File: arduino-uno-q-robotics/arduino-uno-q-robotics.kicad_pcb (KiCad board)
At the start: 4 copper layers, 68.6 x 53.3 mm, 15 parts, among them J1 Conn_02x30_Odd_Even, J2 Conn_02x30_Odd_Even, J3 Connector_FFC-FPC, J5 Conn_02x13_Odd_Even, J6 Conn_02x04_Odd_Even, U1 LSM6DSO32, U2 TCA9803

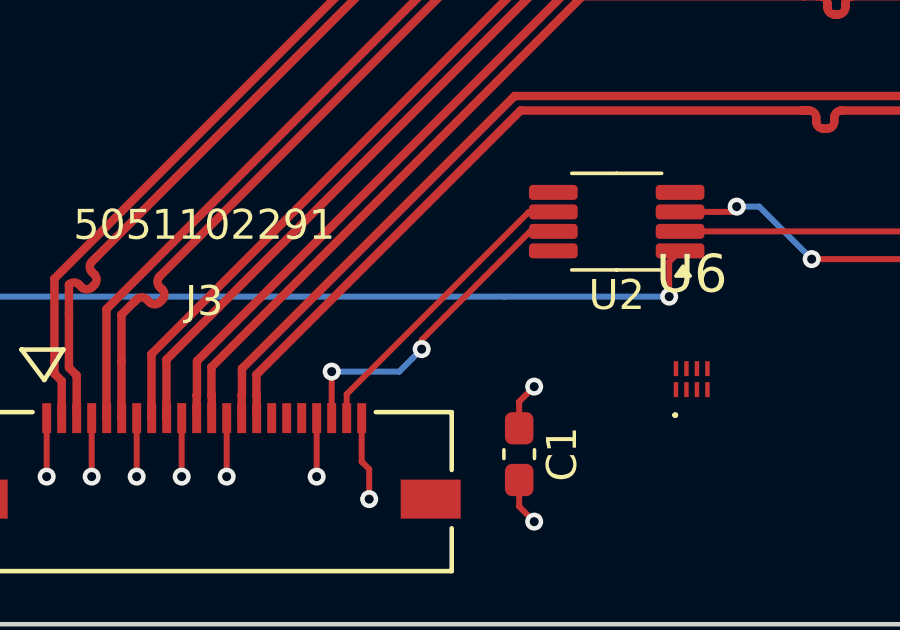
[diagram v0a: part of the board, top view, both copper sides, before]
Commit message: Fix DRC clearance issues
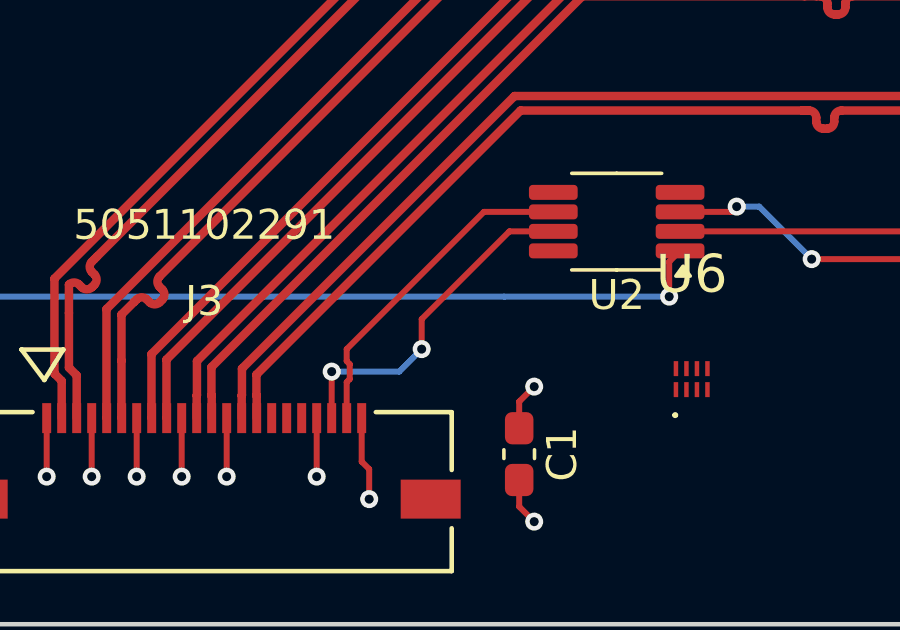
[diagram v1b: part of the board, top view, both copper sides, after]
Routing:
- net /SDA0_3.3V: track 10.2 -> 11.2 mm
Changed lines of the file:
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@@
+	)
+	(segment
+		(start 171.73 108.75)
+		(end 161 108.75)
+		(width 0.2)
+		(layer "F.Cu")
+		(net 56)
+	)
+	(segment
+		(start 172.48 108)
+		(end 171.73 108.75)
+		(width 0.2)
+		(layer "F.Cu")
+		(net 56)
+	)
+	(segment
+		(start 158.5 107)
+		(end 158.325 107.175)
+		(width 0.2)
+		(layer "F.Cu")
+		(net 56)
 	)
 	(segment
@@
 		(net 56)
 	)
-	(segment
-		(start 171.73 108.75)
-		(end 161 108.75)
-		(width 0.2)
-		(layer "F.Cu")
-		(net 56)
-	)
-	(segment
-		(start 158.5 107)
-		(end 158.325 107.175)
-		(width 0.2)
-		(layer "F.Cu")
-		(net 56)
-	)
-	(segment
-		(start 172.48 108)
-		(end 171.73 108.75)
-		(width 0.2)
-		(layer "F.Cu")
-		(net 56)
-	)
 	(via
 		(at 158.5 107)
@@
 	)
 	(segment
-		(start 151.619082 107.825)
-		(end 148 111.444082)
+		(start 150.925 107.825)
+		(end 148 110.75)
+		(width 0.2)
+		(layer "F.Cu")
+		(net 65)
+	)
+	(segment
+		(start 148 110.75)
+		(end 148 111.75)
 		(width 0.2)
 		(layer "F.Cu")
@@
 	(segment
 		(start 152.3875 107.825)
-		(end 151.619082 107.825)
+		(end 150.925 107.825)
 		(width 0.2)
 		(layer "F.Cu")
@@
 		(net 65)
 	)
-	(segment
-		(start 148 111.444082)
-		(end 148 111.75)
-		(width 0.2)
-		(layer "F.Cu")
-		(net 65)
-	)
 	(via
 		(at 148 111.75)
@@
 	)
 	(segment
-		(start 145.500001 113.25)
+		(start 150.075 107.175)
+		(end 145.500001 111.749999)
+		(width 0.2)
+		(layer "F.Cu")
+		(net 68)
+	)
+	(segment
+		(start 145.500001 111.749999)
+		(end 145.500001 112.150058)
+		(width 0.2)
+		(layer "F.Cu")
+		(net 68)
+	)
+	(segment
+		(start 152.3875 107.175)
+		(end 150.075 107.175)
+		(width 0.2)
+		(layer "F.Cu")
+		(net 68)
+	)
+	(segment
+		(start 145.500001 112.150058)
+		(end 145.601 112.251057)
+		(width 0.2)
+		(layer "F.Cu")
+		(net 68)
+	)
+	(segment
+		(start 145.601 112.251057)
+		(end 145.601 112.748943)
+		(width 0.2)
+		(layer "F.Cu")
+		(net 68)
+	)
+	(segment
+		(start 145.601 112.748943)
+		(end 145.500001 112.849942)
+		(width 0.2)
+		(layer "F.Cu")
+		(net 68)
+	)
+	(segment
+		(start 145.500001 112.849942)
 		(end 145.500001 114.05)
 		(width 0.2)
 		(layer "F.Cu")
-		(net 68)
-	)
-	(segment
-		(start 151.575001 107.175)
-		(end 145.500001 113.25)
-		(width 0.2)
-		(layer "F.Cu")
-		(net 68)
-	)
-	(segment
-		(start 152.3875 107.175)
-		(end 151.575001 107.175)
-		(width 0.2)
-		(layer "F.Cu")

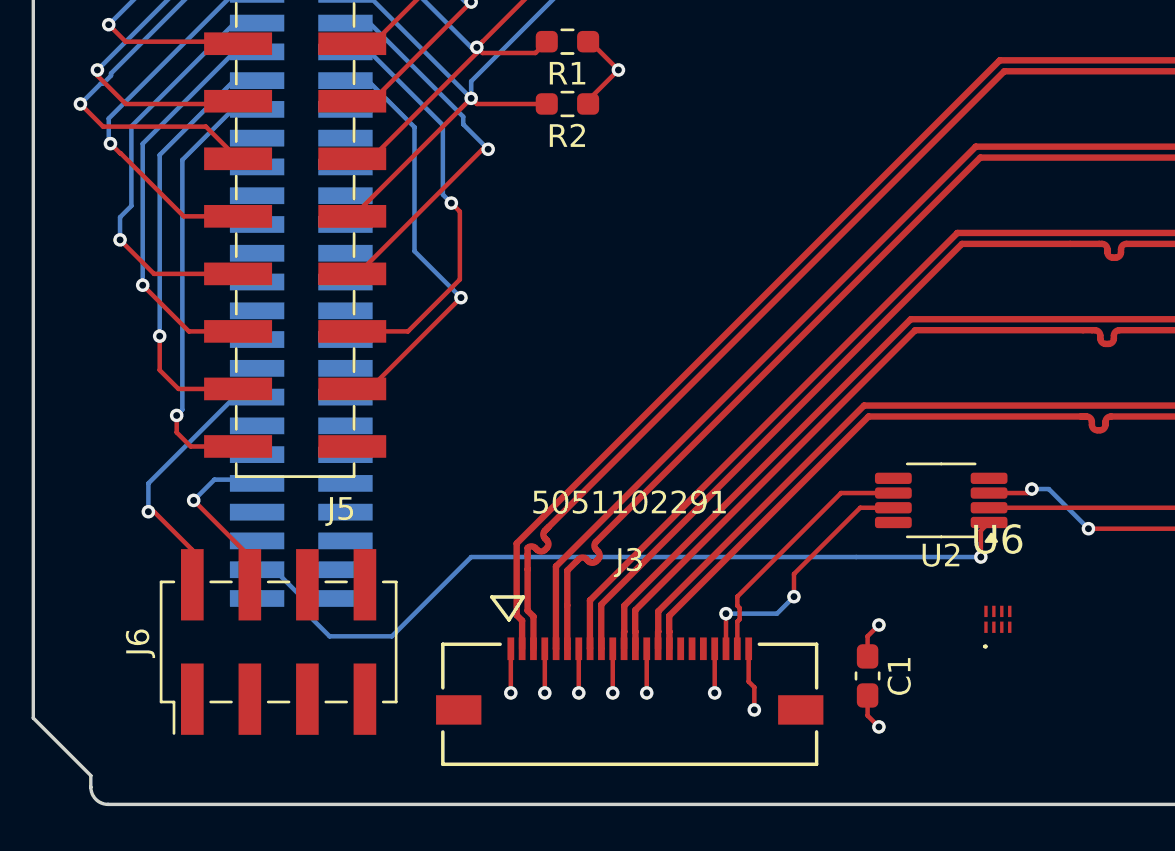
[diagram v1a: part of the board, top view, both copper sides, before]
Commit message: Add male header for JMISC ports
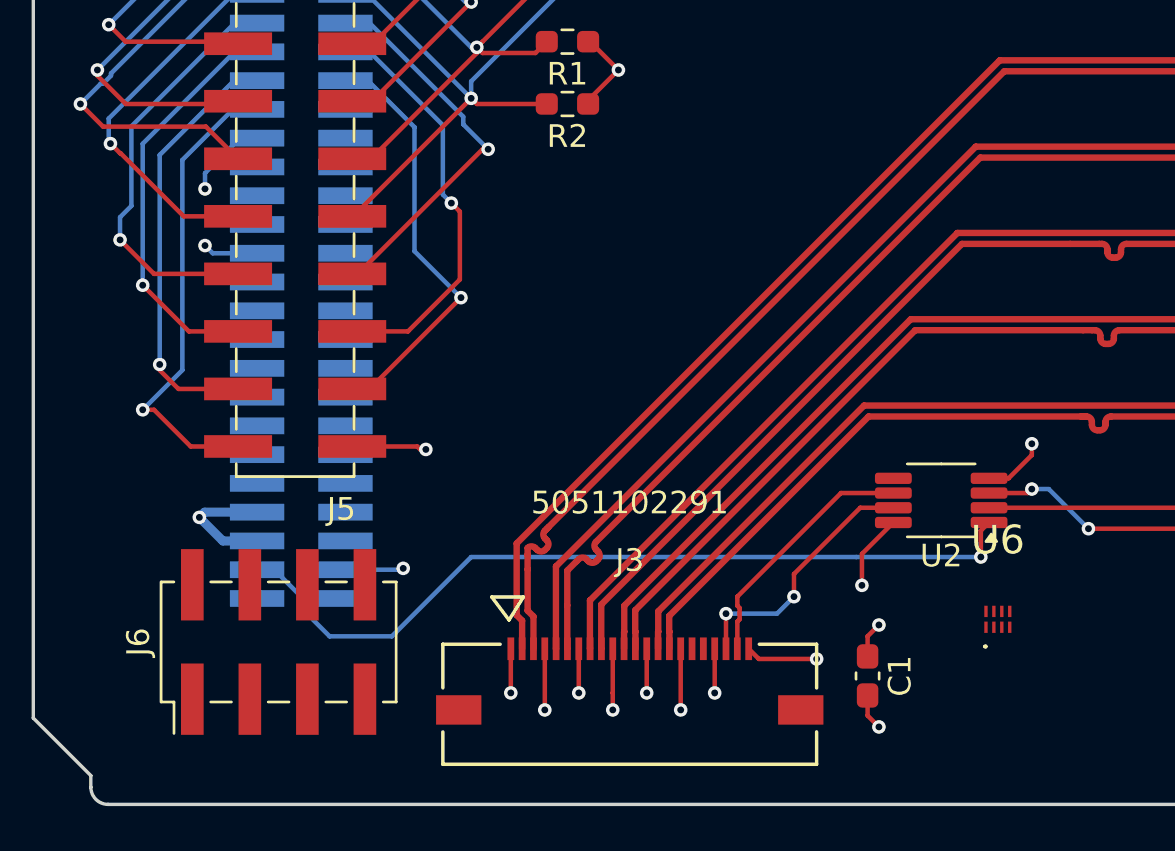
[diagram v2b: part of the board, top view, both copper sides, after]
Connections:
- J6 pad 4: /SOC_GPIO_28 -> /SOC_GPIO_82_SE0
- J6 pad 8: /SOC_GPIO_82_SE0 -> /SOC_GPIO_28
- U6 pad 8: unconnected-(U6-VCCB-Pad8) -> +3.3V
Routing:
- net GND: track 22.1 -> 41.1 mm, vias 9 -> 15
- net /SOC_GPIO_86_SE0: track 11.9 -> 0.00 mm, vias 1 -> 0
- net +3.3V: track 15.3 -> 24.6 mm, vias 5 -> 7
- net /SOC_GPIO_28: track 7.93 -> 0.23 mm, vias 1 -> 0
- net /MCU_CRS_SYNC: track 19.4 -> 20.9 mm
- net /SOC_GPIO_18: track 0.00 -> 0.83 mm

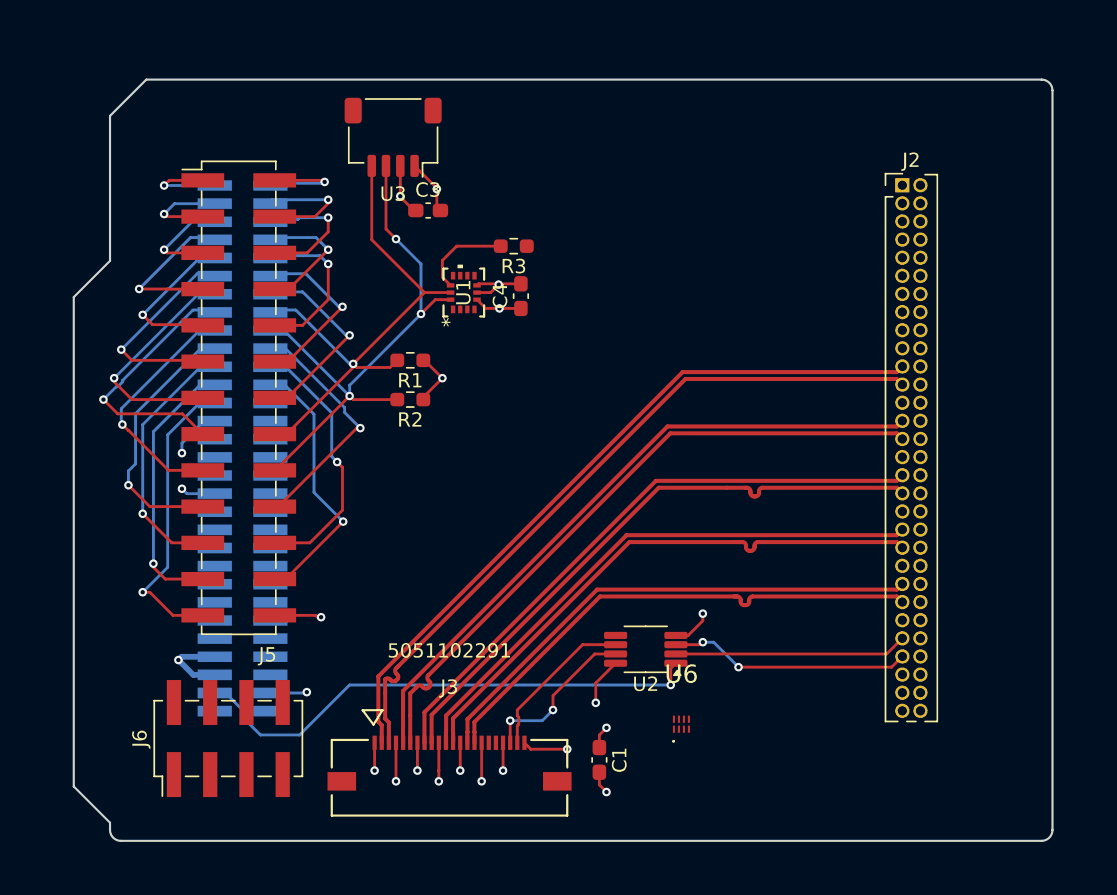
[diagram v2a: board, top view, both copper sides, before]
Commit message: Adjust JMISC male headers position
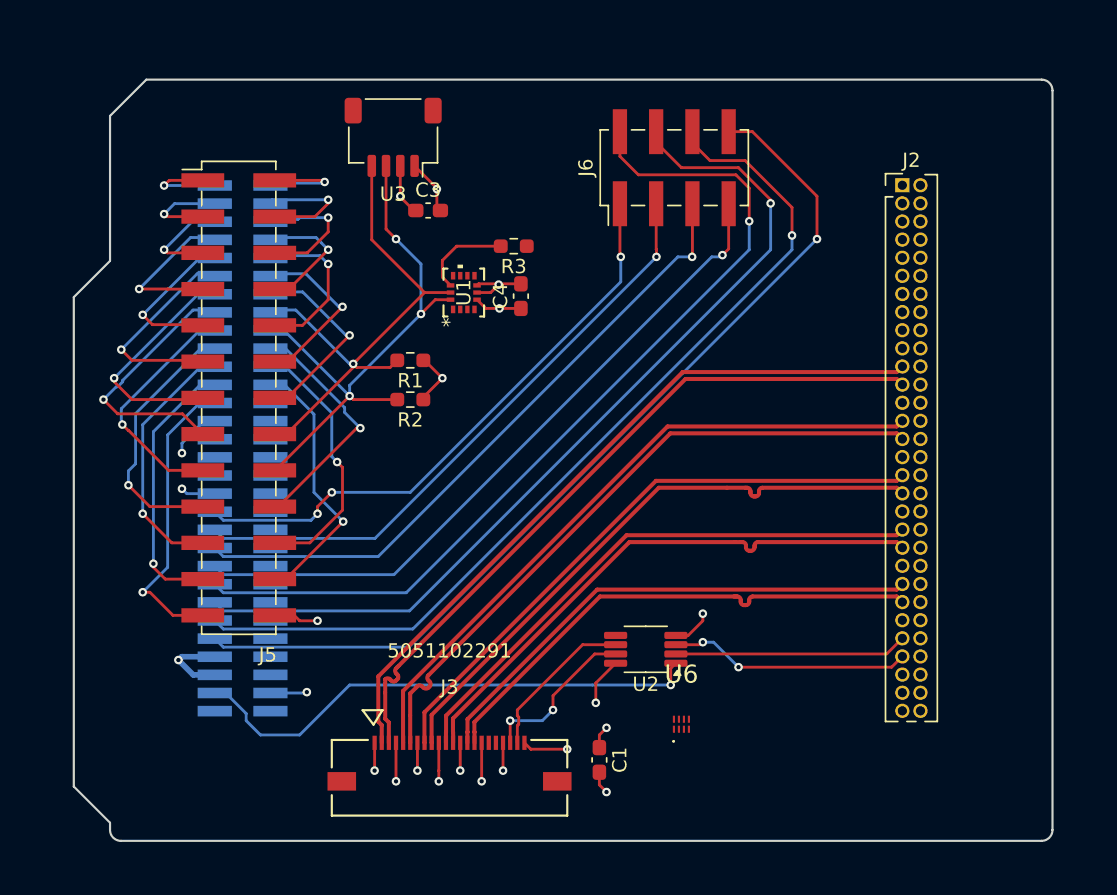
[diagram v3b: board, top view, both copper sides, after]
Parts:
- moved J6 50.8 mm to (156.5, 73.8)
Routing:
- net /SOC_GPIO_28: track 0.23 -> 65.6 mm, vias 0 -> 1
- net /SOC_GPIO_18: track 0.83 -> 65.1 mm, vias 0 -> 1
- net /SOC_GPIO_86_SE0: track 0.00 -> 63.7 mm, vias 0 -> 1
- net /SOC_GPIO_82_SE0: track 0.00 -> 63.6 mm, vias 0 -> 1
- net /SOC_GPIO_3_SE0: track 0.00 -> 48.9 mm, vias 0 -> 1
- net /SOC_GPIO_2_SE0: track 0.00 -> 46.1 mm, vias 0 -> 1
- net /SOC_GPIO_1_SE0: track 0.00 -> 43.1 mm, vias 0 -> 1
- net /SOC_GPIO_0_SE0: track 0.00 -> 41.4 mm, vias 0 -> 3

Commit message: Add missing pin functions to JMISC/MEDIA
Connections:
- J1 pad 44: unconnected-(J1-Pin_44-Pad44) -> GND
- J2 pad 57: unconnected-(J2-Pin_57-Pad57) -> VIN
- J2 pad 59: unconnected-(J2-Pin_59-Pad59) -> VIN

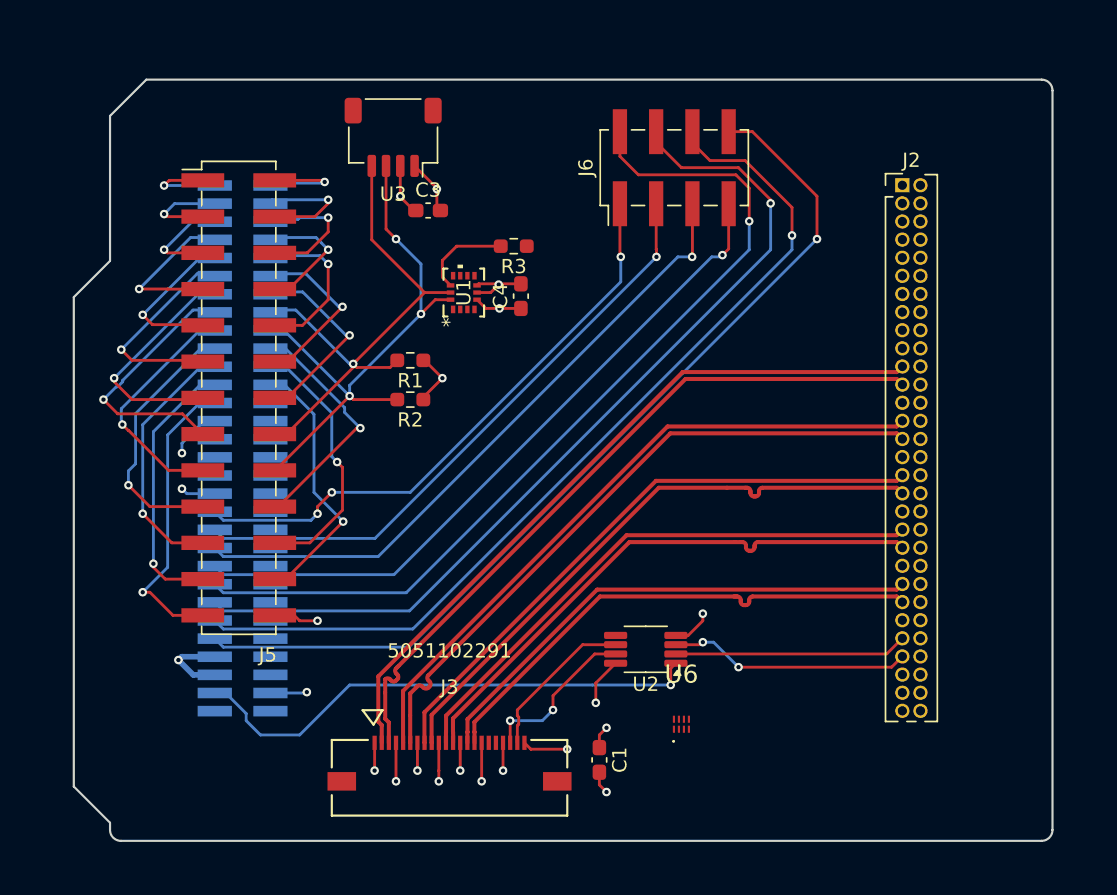
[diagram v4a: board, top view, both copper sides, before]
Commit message: Move silkscreen to fab layer
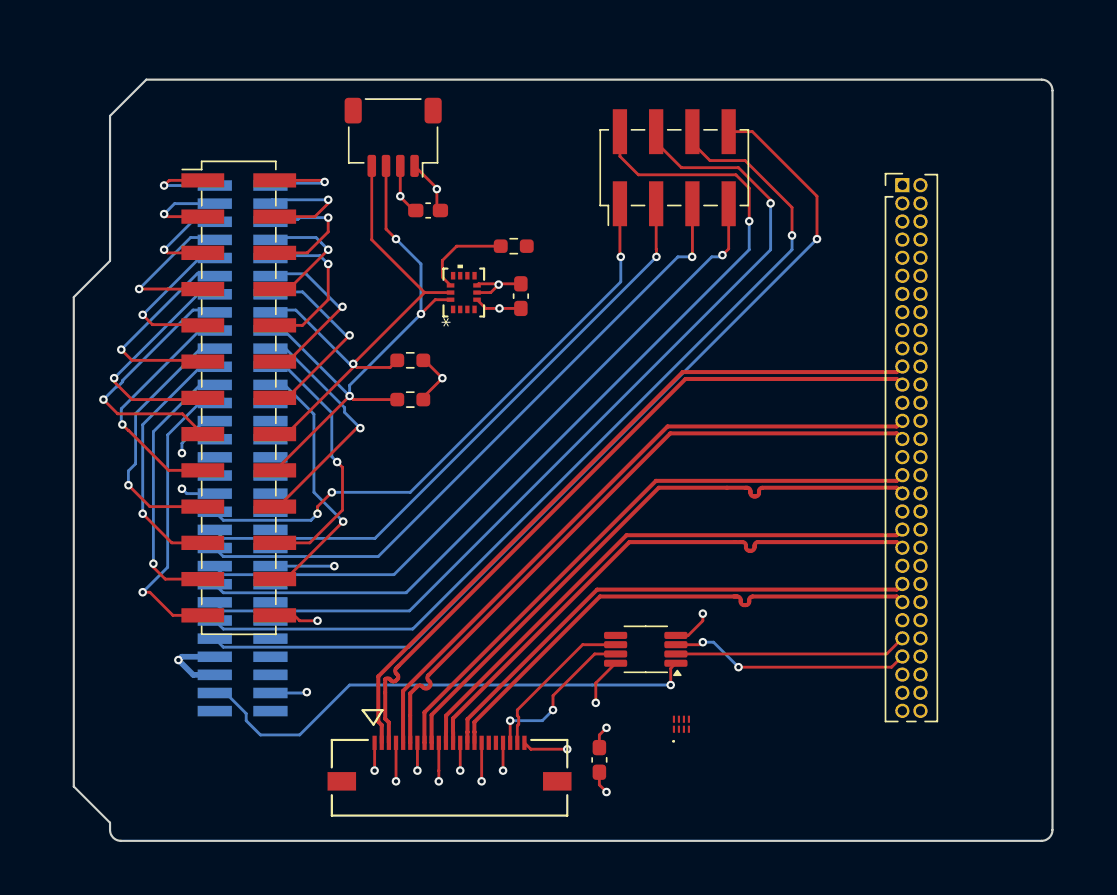
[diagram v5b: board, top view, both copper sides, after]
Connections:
- J2 pad 58: +3V3 -> +3.3V
- J2 pad 60: +3V3 -> +3.3V
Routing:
- net GND: track 40.9 -> 45.4 mm, vias 15 -> 16

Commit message: Fix DRC warnings/errors
Fix DRC errors
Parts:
- moved U6 0.50 mm to (156.5, 112.8), turned to 90 degrees
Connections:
- J1 pad 26: VBAT -> GND
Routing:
- net /SOC_CAM_MCLK0: track 0.00 -> 50.3 mm
- net +3.3V: track 24.6 -> 32.2 mm, vias 7 -> 9
- net +1V8: track 36.6 -> 42.7 mm, vias 1 -> 2
- net GND: track 45.4 -> 49.6 mm, vias 16 -> 18
- net VBUS: track 0.00 -> 1.27 mm
- net VIN: track 0.00 -> 1.27 mm
